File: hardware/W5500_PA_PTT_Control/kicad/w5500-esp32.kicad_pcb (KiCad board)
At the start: 2 copper layers, 18 parts, among them J1 ESP32_DevKitC_Socket_40P_25.4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, Q1 2SC1815, Q3 2SC1815, Q5 2SJ334, U1 TA48033S, U2 L7805

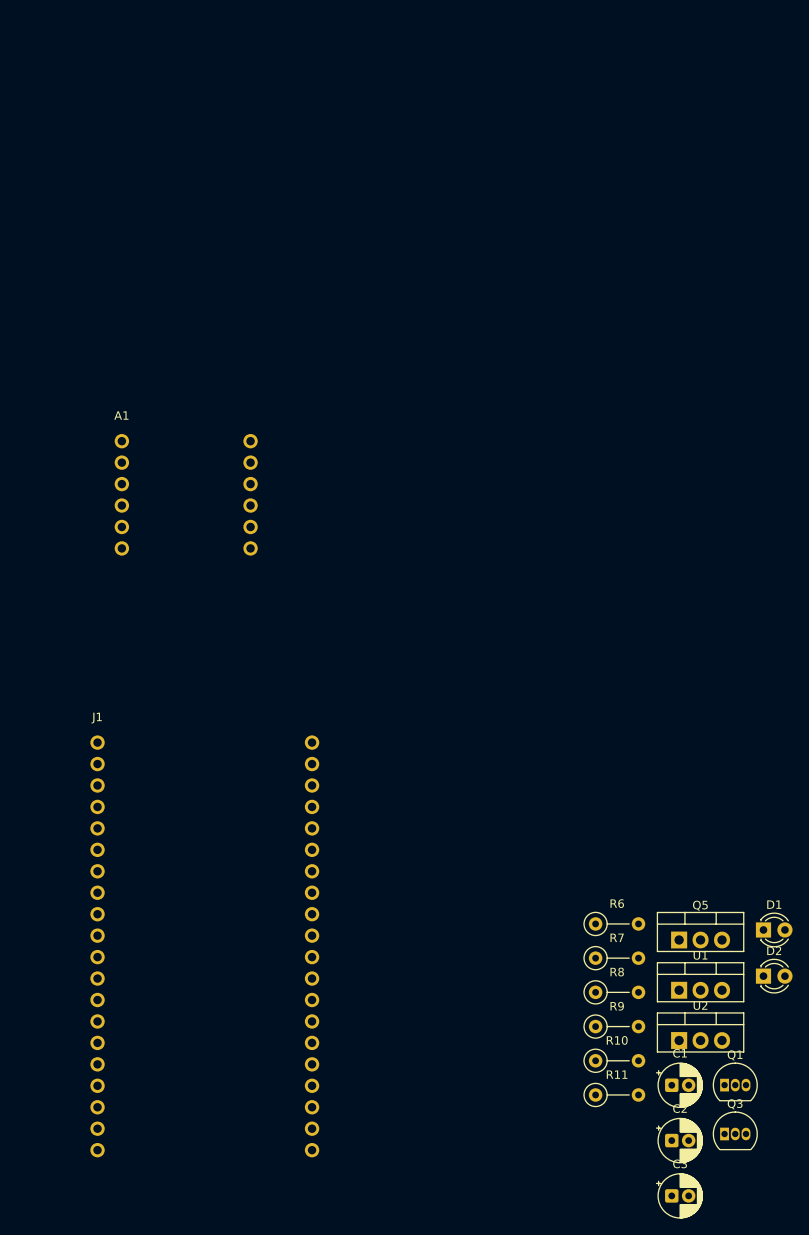
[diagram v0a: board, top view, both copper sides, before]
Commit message: PA/PTTコントローラの基板・資料をPi5版のRev.2.6に更新し、READMEに説明を追加
KiCadデータ・JLCPCB発注データ・日英併記の仕様書と接続一覧(Windows版の連携に
合わせて4.4節を記述)を入れ、READMEに日英併記の節を追加した。

Co-Authored-By: Claude Opus 5.5 <noreply@anthropic.com>
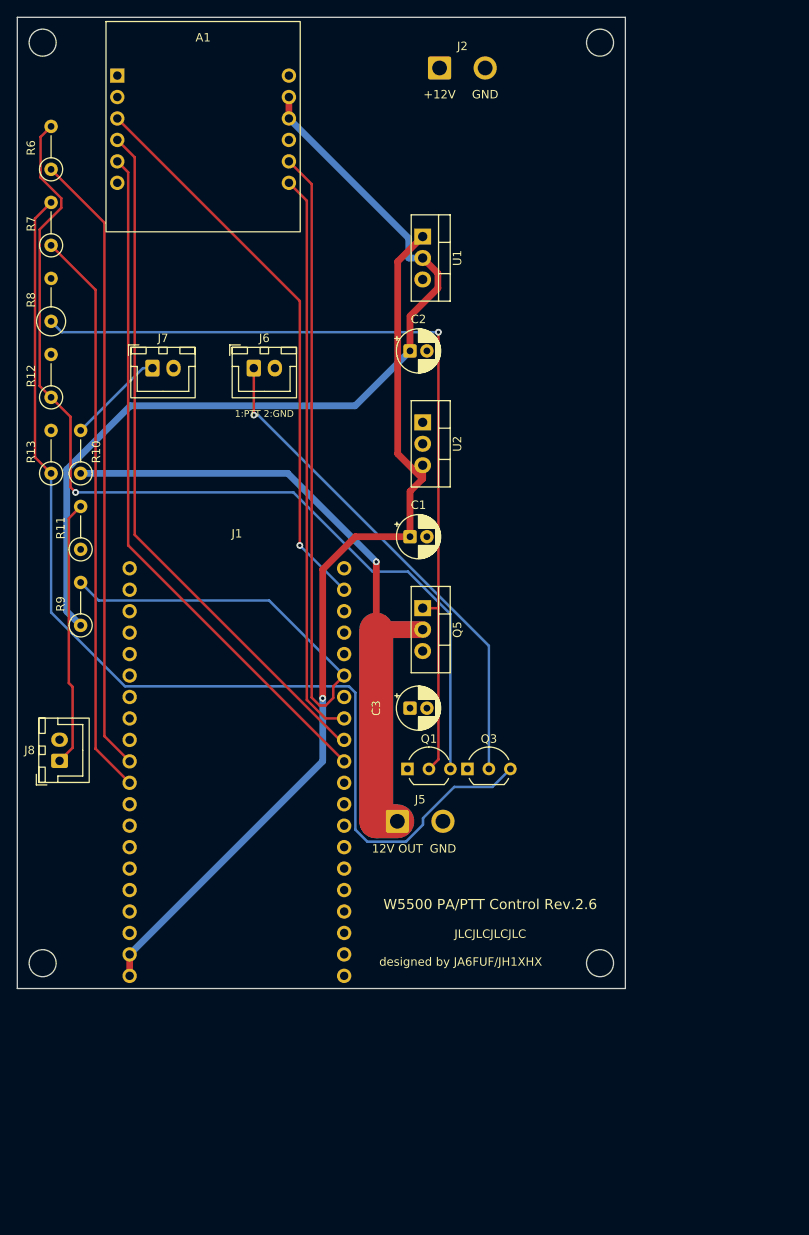
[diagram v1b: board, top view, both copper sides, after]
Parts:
- removed D1: LED_Red_3mm, LED_THT:LED_D3.0mm
- removed D2: LED_Green_3mm, LED_THT:LED_D3.0mm
- added H1: MountingHole_3.2mm_M3, MountingHole:MountingHole_3.2mm_M3, F.Cu at (67.0, 49.5)
- added H2: MountingHole_3.2mm_M3, MountingHole:MountingHole_3.2mm_M3, F.Cu at (133.0, 49.5)
- added H3: MountingHole_3.2mm_M3, MountingHole:MountingHole_3.2mm_M3, F.Cu at (67.0, 158.5)
- added H4: MountingHole_3.2mm_M3, MountingHole:MountingHole_3.2mm_M3, F.Cu at (133.0, 158.5)
- added J2: DC_IN_13V8, Connector_Wire:SolderWire-1sqmm_1x02_P5.4mm_D1.4mm_OD2.7mm, F.Cu at (114.0, 52.5)
- added J5: Power, Connector_Wire:SolderWire-1sqmm_1x02_P5.4mm_D1.4mm_OD2.7mm, F.Cu at (109.0, 141.7)
- added J6: PTT_ON, Connector_JST:JST_XH_B2B-XH-A_1x02_P2.50mm_Vertical, F.Cu at (92.0, 88.0)
- added J7: LED_PWR, Connector_JST:JST_XH_B2B-XH-A_1x02_P2.50mm_Vertical, F.Cu at (80.0, 88.0)
- added J8: LED_12V, Connector_JST:JST_XH_B2B-XH-A_1x02_P2.50mm_Vertical, F.Cu at (69.0, 134.5)
- added R12: 10k, Resistor_THT:R_Axial_DIN0207_L6.3mm_D2.5mm_P5.08mm_Vertical, F.Cu at (68.0, 91.5)
- added R13: 10k, Resistor_THT:R_Axial_DIN0207_L6.3mm_D2.5mm_P5.08mm_Vertical, F.Cu at (68.0, 100.5)
- A1: footprint project_footprints:W5500_Lite_2x06_P2.54mm_15.24mm -> project_footprints:W5500_Lite_USR-ES1_2x06_P2.54mm_20.32mm
- C1, C3: value 0.1uF -> 0.33uF
- C2: value 0.1uF -> 33uF
- Q1, Q3: footprint Package_TO_SOT_THT:TO-92_Inline -> Package_TO_SOT_THT:TO-92_Inline_Wide
- R8: value 10k -> 1k; footprint Resistor_THT:R_Axial_DIN0207_L6.3mm_D2.5mm_P5.08mm_Vertical -> Resistor_THT:R_Axial_DIN0309_L9.0mm_D3.2mm_P5.08mm_Vertical
- moved R6 110.2 mm to (68.0, 64.5), turned to 90 degrees
- moved R7 106.2 mm to (68.0, 73.5), turned to 90 degrees
- moved R8 102.3 mm to (68.0, 82.5), turned to 90 degrees
- moved C2 98.5 mm to (110.5, 86.0)
- moved U1 94.3 mm to (112.0, 72.4), turned to -90 degrees
- moved R10 92.5 mm to (71.5, 100.5), turned to 90 degrees
- moved R11 88.8 mm to (71.5, 109.5), turned to 90 degrees
- moved U2 79.2 mm to (112.0, 94.4), turned to -90 degrees
- moved R9 77.3 mm to (71.5, 118.5), turned to 90 degrees
- moved C1 72.0 mm to (110.5, 108.0)
- moved C3 65.5 mm to (110.5, 128.3)
- moved Q1 53.0 mm to (110.2, 135.5)
- moved Q3 52.9 mm to (117.3, 135.5)
- moved Q5 49.7 mm to (112.0, 116.4), turned to -90 degrees
- moved A1 43.3 mm to (75.8, 53.4)
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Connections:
- J1 pad 21: unconnected-(J1-GND-Pad21) -> GND
- J1 pad 22: unconnected-(J1-GND-Pad22) -> GND
- J1 pad 23: unconnected-(J1-GND-Pad23) -> GND
- J1 pad 24: unconnected-(J1-GND-Pad24) -> GND
- J1 pad 40: unconnected-(J1-GND-Pad40) -> GND
- J1 pad 7: <NO NET> -> GND
- Q5 pad 1: (no net) -> Net-(Q1-C)
- Q5 pad 2: (no net) -> /Power
- Q5 pad 3: (no net) -> +12V
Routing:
- net Net-(Q3-B): track 0.00 -> 129.3 mm
- net Net-(Q1-B): track 0.00 -> 116.4 mm, vias 0 -> 1
- net /+5v0: track 0.00 -> 109.8 mm, vias 0 -> 1
- net /Power: track 0.00 -> 108.8 mm, vias 0 -> 1
- net /GPIO21_W5500_RST: track 0.00 -> 106.9 mm
- net /+3V3_A: track 0.00 -> 105.3 mm
- net Net-(Q1-C): track 0.00 -> 100.4 mm, vias 0 -> 1
- net Net-(A1-SCK): track 0.00 -> 82.5 mm
- net Net-(A1-CS): track 0.00 -> 82.2 mm
- net /GPIO26_PA: track 0.00 -> 74.0 mm
- net /GPIO27_PTT: track 0.00 -> 67.5 mm
- net Net-(A1-MISO): track 0.00 -> 67.4 mm
- net Net-(A1-MOSI): track 0.00 -> 66.9 mm, vias 0 -> 1
- net /PTT_ON: track 0.00 -> 59.3 mm, vias 0 -> 1
- net Net-(J8-Pin_1): track 0.00 -> 31.5 mm
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- added copper zone on In2.Cu, net +12V
- added copper zone on In1.Cu, net GND
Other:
- board outline added: 72 x 115 mm
- copper layers 2 -> 4
- board text added: "+12V"
- board text added: "12V OUT"
- board text added: "1:PTT 2:GND"
- board text added: "Freenove ESP32 WROOM 約27x58.5(要実測)"
- board text added: "GND"
- board text added: "JLCJLCJLCJLC"
- board text added: "W5500 Lite (USR-ES1) 23x25"
- board text added: "W5500 PA/PTT Control Rev.2.6"
- board text added: "designed by JA6FUF/JH1XHX"
- board text added: "ケース内壁 80x120"
- board text added: "前面 RJ45開口 x45-63 z10-24"
- board text added: "前面 丸穴 Ø16 z17.5"
- board text added: "前面コネクタ裏 空き 20mm(配線用)"
- board text added: "放熱器 Q5 20x20 (M3穴 高さ18)"
- board text added: "放熱器 U1 20x20 (M3穴 高さ18)"
- board text added: "放熱器 U2 20x20 (M3穴 高さ18)"
- board text added: "背面 USB-C開口 15x6 z7"
- board text added: "背面 丸穴 Ø16 z17.5"
- board text added: "背面コネクタ裏 空き 20mm(配線用)"
